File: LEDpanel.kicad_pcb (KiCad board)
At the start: 2 copper layers, 100 x 100 mm, 107 parts, among them J1 Barrel_Jack_Switch, J2 Barrel_Jack_Switch, J3 Conn_01x02, SW1 SW_SPST, U1 LM317_TO-252, U2 LM317_TO-252, U3 LM317_TO-252, U4 LM317_TO-252, U5 LM317_TO-252, U6 LM317_TO-252

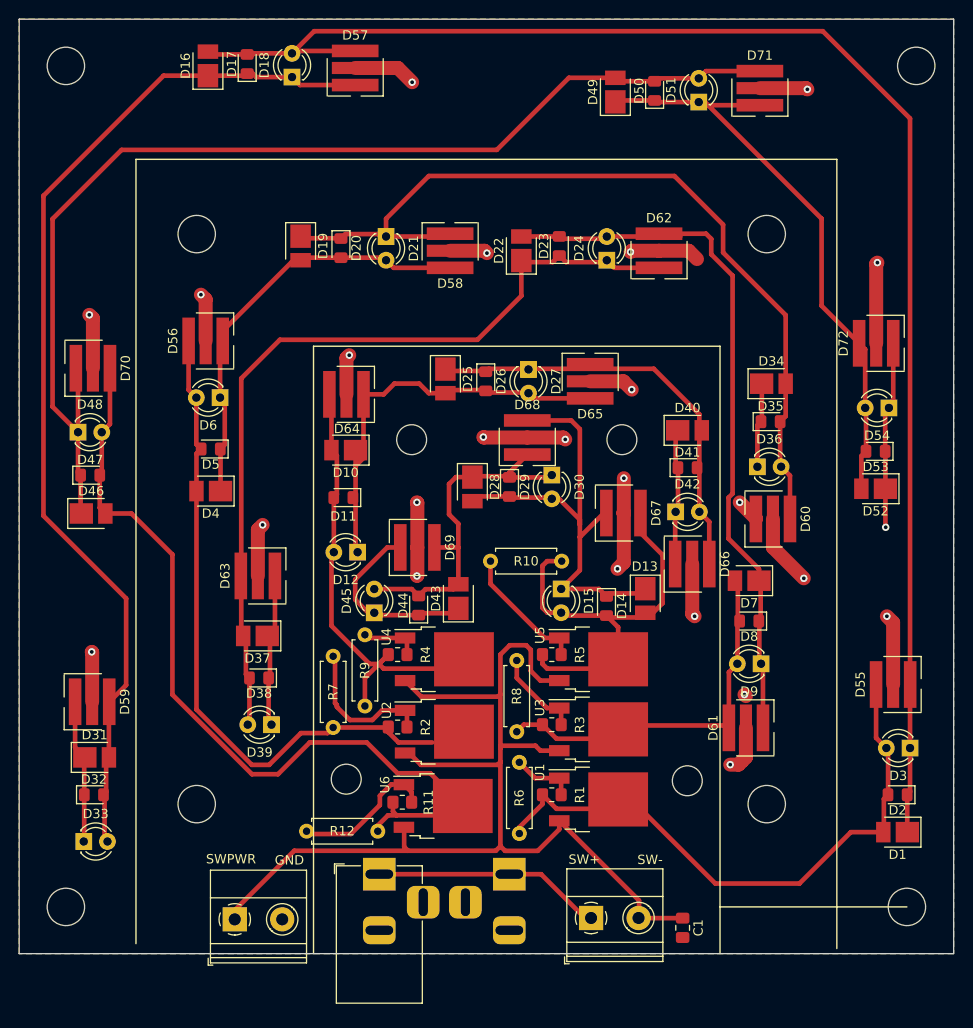
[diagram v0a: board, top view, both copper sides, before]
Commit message: Distributed the components somewhat better
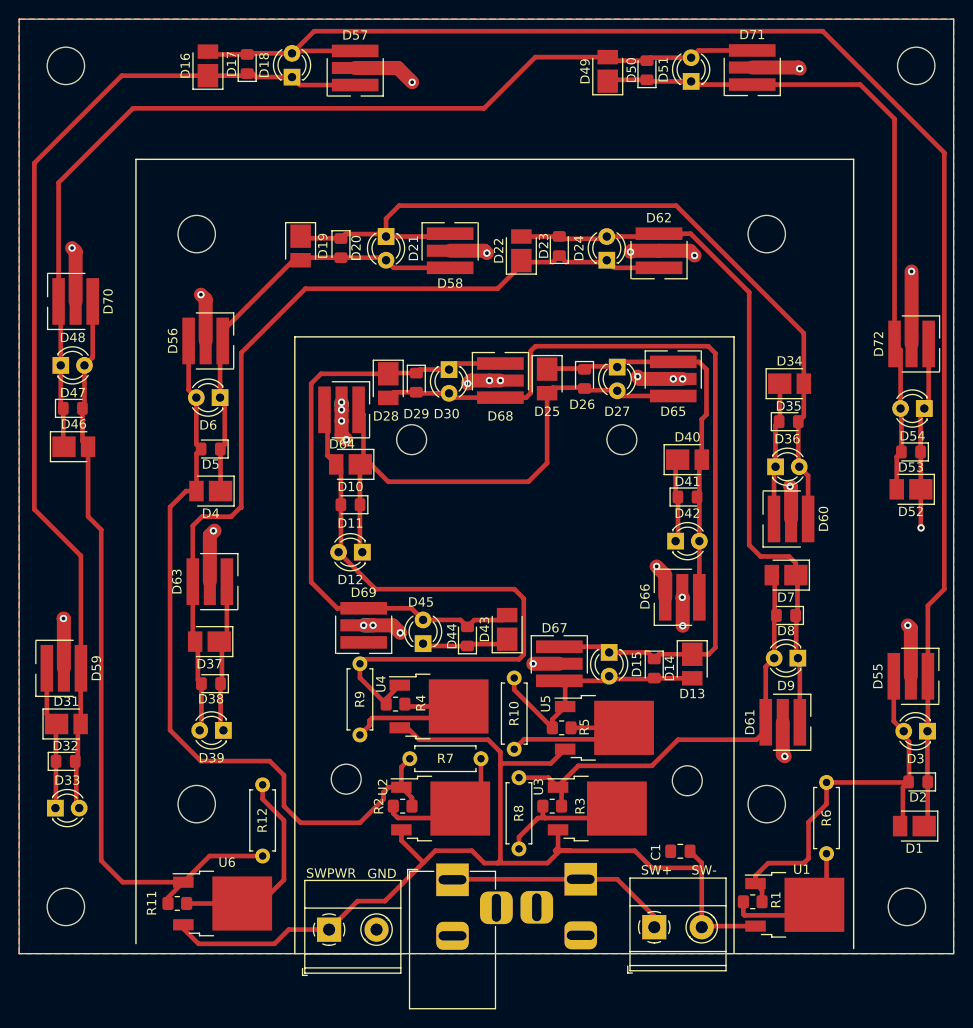
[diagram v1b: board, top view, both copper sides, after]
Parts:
- moved R6 32.9 mm to (111.4, 114.3)
- moved R11 26.4 mm to (41.9, 119.6), turned to 180 degrees
- moved U6 25.8 mm to (46.8, 119.6)
- moved R1 24.4 mm to (103.5, 119.5)
- moved U1 23.8 mm to (108.0, 119.8)
- moved R10 20.8 mm to (78.0, 103.1), turned to 90 degrees
- moved D67 17.5 mm to (82.8, 94.0), turned to -90 degrees
- moved R7 16.2 mm to (74.4, 104.1), turned to 180 degrees
- moved D30 15.8 mm to (71.0, 62.5)
- moved D29 15.0 mm to (67.5, 63.9)
- moved D28 14.3 mm to (64.5, 64.0)
- moved R12 13.3 mm to (51.1, 106.9), turned to -90 degrees
- moved R8 12.5 mm to (78.5, 113.8)
- moved D25 10.9 mm to (81.5, 63.5)
- moved D26 10.6 mm to (85.5, 63.5)
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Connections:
- D1 pad 2: Net-(D1-Pad2) -> Net-(R1-Pad2)
- D10 pad 2: Net-(D10-Pad2) -> Net-(R4-Pad2)
- D11 pad 2: Net-(D10-Pad2) -> Net-(R4-Pad2)
- D12 pad 2: Net-(D10-Pad2) -> Net-(R4-Pad2)
- D2 pad 2: Net-(D1-Pad2) -> Net-(R1-Pad2)
- D3 pad 2: Net-(D1-Pad2) -> Net-(R1-Pad2)
- D55 pad 2: Net-(D1-Pad2) -> Net-(R1-Pad2)
- D61 pad 2: Net-(D7-Pad2) -> Net-(R3-Pad2)
- D64 pad 2: Net-(D10-Pad2) -> Net-(R4-Pad2)
- D7 pad 2: Net-(D7-Pad2) -> Net-(R3-Pad2)
- D8 pad 2: Net-(D7-Pad2) -> Net-(R3-Pad2)
- D9 pad 2: Net-(D7-Pad2) -> Net-(R3-Pad2)
- R1 pad 1: Net-(D1-Pad2) -> Net-(R1-Pad1)
- R10 pad 1: Net-(D13-Pad2) -> Net-(R10-Pad1)
- R10 pad 2: Net-(R10-Pad2) -> Net-(D13-Pad2)
- R11 pad 1: Net-(D46-Pad2) -> Net-(R11-Pad1)
- R11 pad 2: Net-(R11-Pad2) -> Net-(D46-Pad2)
- R12 pad 1: Net-(D46-Pad2) -> Net-(R11-Pad1)
- R12 pad 2: Net-(R11-Pad2) -> Net-(D46-Pad2)
- R2 pad 1: Net-(D4-Pad2) -> Net-(R2-Pad1)
- R2 pad 2: Net-(R2-Pad2) -> Net-(D4-Pad2)
- R3 pad 1: Net-(D7-Pad2) -> Net-(R3-Pad1)
- R4 pad 1: Net-(D10-Pad2) -> Net-(R4-Pad1)
- R5 pad 1: Net-(D13-Pad2) -> Net-(R10-Pad1)
- R5 pad 2: Net-(R10-Pad2) -> Net-(D13-Pad2)
- R6 pad 1: Net-(D1-Pad2) -> Net-(R1-Pad1)
- R7 pad 1: Net-(D4-Pad2) -> Net-(R2-Pad1)
- R7 pad 2: Net-(R2-Pad2) -> Net-(D4-Pad2)
- R8 pad 1: Net-(D7-Pad2) -> Net-(R3-Pad1)
- R9 pad 1: Net-(D10-Pad2) -> Net-(R4-Pad1)
- U1 pad 2: Net-(D1-Pad2) -> Net-(R1-Pad1)
- U2 pad 1: Net-(R2-Pad2) -> Net-(D4-Pad2)
- U2 pad 2: Net-(D4-Pad2) -> Net-(R2-Pad1)
- U3 pad 2: Net-(D7-Pad2) -> Net-(R3-Pad1)
- U4 pad 2: Net-(D10-Pad2) -> Net-(R4-Pad1)
- U5 pad 1: Net-(R10-Pad2) -> Net-(D13-Pad2)
- U5 pad 2: Net-(D13-Pad2) -> Net-(R10-Pad1)
- U6 pad 1: Net-(R11-Pad2) -> Net-(D46-Pad2)
- U6 pad 2: Net-(D46-Pad2) -> Net-(R11-Pad1)
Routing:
- net Net-(R4-Pad2): track 6.30 -> 70.0 mm
- net Net-(D1-Pad2): track 61.7 -> 0.00 mm
- net Net-(D10-Pad2): track 49.8 -> 0.00 mm
- net Net-(D7-Pad2): track 40.8 -> 0.00 mm
- net Net-(R3-Pad2): track 9.62 -> 48.9 mm
- net Net-(D13-Pad1): track 50.8 -> 90.0 mm
- net Net-(R1-Pad2): track 6.84 -> 44.3 mm
- net GND: track 215.2 -> 179.0 mm, vias 24 -> 31
- net Net-(D28-Pad1): track 38.3 -> 65.9 mm
- net Net-(R11-Pad1): track 0.00 -> 22.6 mm
- net Net-(D13-Pad2): track 46.2 -> 27.5 mm
- net Net-(R10-Pad1): track 0.00 -> 18.4 mm
- net Net-(R4-Pad1): track 0.00 -> 18.0 mm
- net Net-(R2-Pad2): track 15.8 -> 0.00 mm
- net Net-(R11-Pad2): track 15.6 -> 0.00 mm
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
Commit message: Distributed the components somewhat better
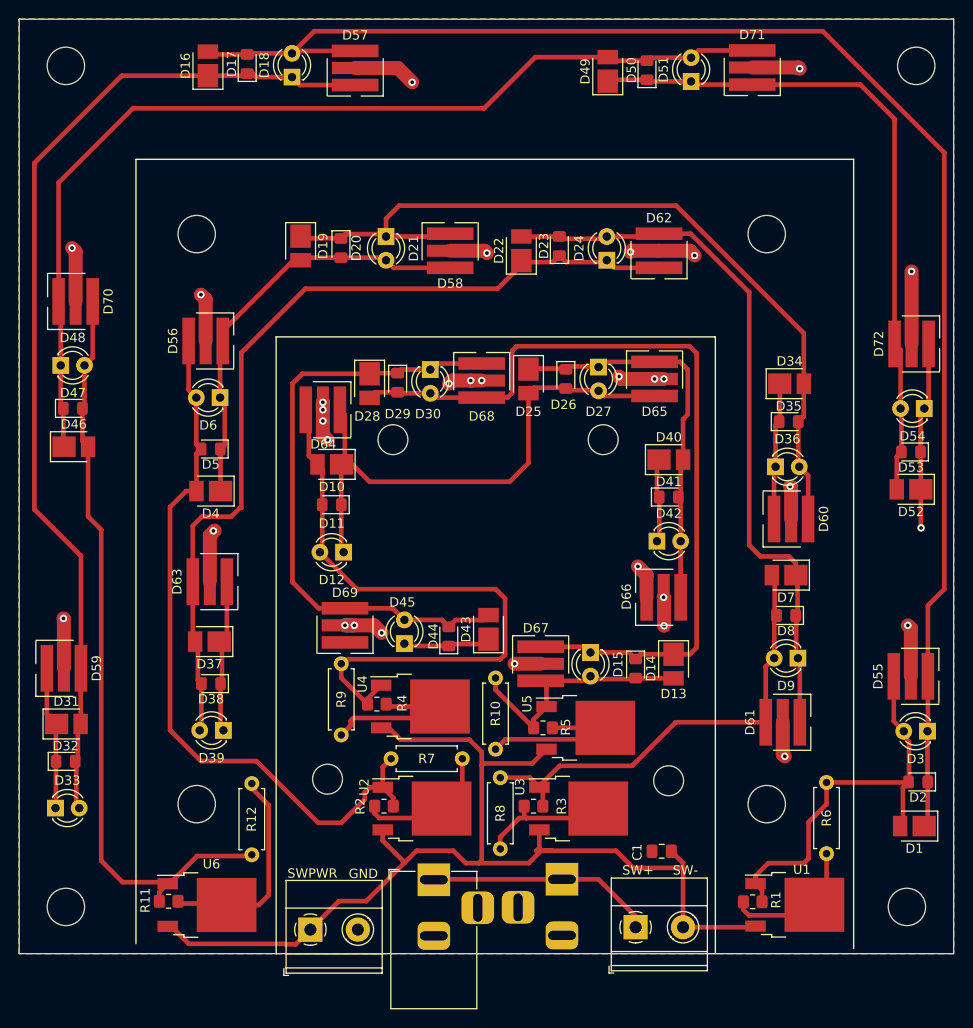
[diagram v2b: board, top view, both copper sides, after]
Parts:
- moved R4 2.00 mm to (63.3, 98.3)
- moved C1 2.00 mm to (93.8, 114.0)
- moved D10 2.00 mm to (58.5, 72.6)
- moved D11 2.00 mm to (58.5, 77.0)
- moved D12 2.00 mm to (59.7, 82.0)
- moved D13 2.00 mm to (95.0, 94.0)
- moved D14 2.00 mm to (91.0, 94.5)
- moved D15 2.00 mm to (86.1, 92.8)
- moved D25 2.00 mm to (79.5, 63.5)
- moved D26 2.00 mm to (83.5, 63.5)
- moved D27 2.00 mm to (87.0, 62.2)
- moved D28 2.00 mm to (62.5, 64.0)
- moved D29 2.00 mm to (65.5, 63.9)
- moved D30 2.00 mm to (69.0, 62.5)
- moved D40 2.00 mm to (94.5, 72.1)
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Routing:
- net Net-(D4-Pad2): track 83.0 -> 79.0 mm
- net Net-(D46-Pad2): track 83.5 -> 81.8 mm
- net Net-(R3-Pad2): track 48.9 -> 50.4 mm
- net Net-(C1-Pad1): track 117.0 -> 118.4 mm

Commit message: Added silkscreen
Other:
- board text added: "THROUGH-HOLE LEDS: LONG LEAD INTO ROUND HOLE, SHORT LEAD SQUARE HOLE SURFACE MOUNT LEDS: SIDE WITH SILKSCREEN LINES IS CATHODE (NEG)"
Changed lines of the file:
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@@
     )
   )
+  (gr_line (start 37.5 40) (end 37.5 123.93) (layer "B.SilkS") (width 0.15))
+  (gr_line (start 114.3 124.46) (end 114.3 40) (layer "B.SilkS") (width 0.15))
+  (gr_line (start 37.5 40) (end 114.3 40) (layer "B.SilkS") (width 0.15))
+  (gr_line (start 52.5 59) (end 99.5 59) (layer "B.SilkS") (width 0.15))
+  (gr_line (start 99.5 125) (end 99.5 59) (layer "B.SilkS") (width 0.15))
+  (gr_line (start 52.5 59) (end 52.5 125.028) (layer "B.SilkS") (width 0.15))
   (gr_line (start 37.5 123.93) (end 37.5 40) (layer "F.SilkS") (width 0.15))
   (gr_line (start 52.5 59) (end 99.5 59) (layer "F.SilkS") (width 0.15))
@@
   (gr_line (start 25 125) (end 25 25) (layer "Edge.Cuts") (width 0.1))
   (gr_line (start 25 25) (end 125 25) (layer "Edge.Cuts") (width 0.1))
+  (gr_text "THROUGH-HOLE LEDS: LONG LEAD INTO\nROUND HOLE, SHORT LEAD SQUARE HOLE\nSURFACE MOUNT LEDS: SIDE WITH\nSILKSCREEN LINES IS CATHODE (NEG)" (at 76 79.5) (layer "B.SilkS")
+    (effects (font (size 1 1) (thickness 0.15)) (justify mirror))
+  )
   (gr_text "SW-" (at 96.298 116.078) (layer "F.SilkS")
     (effects (font (size 1 1) (thickness 0.15)))
